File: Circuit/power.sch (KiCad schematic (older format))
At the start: 20 parts, among them Q202 FDN340P, Q203 FDN340P, U201 CN3063, U202 MCP6002, U4 LD3985M

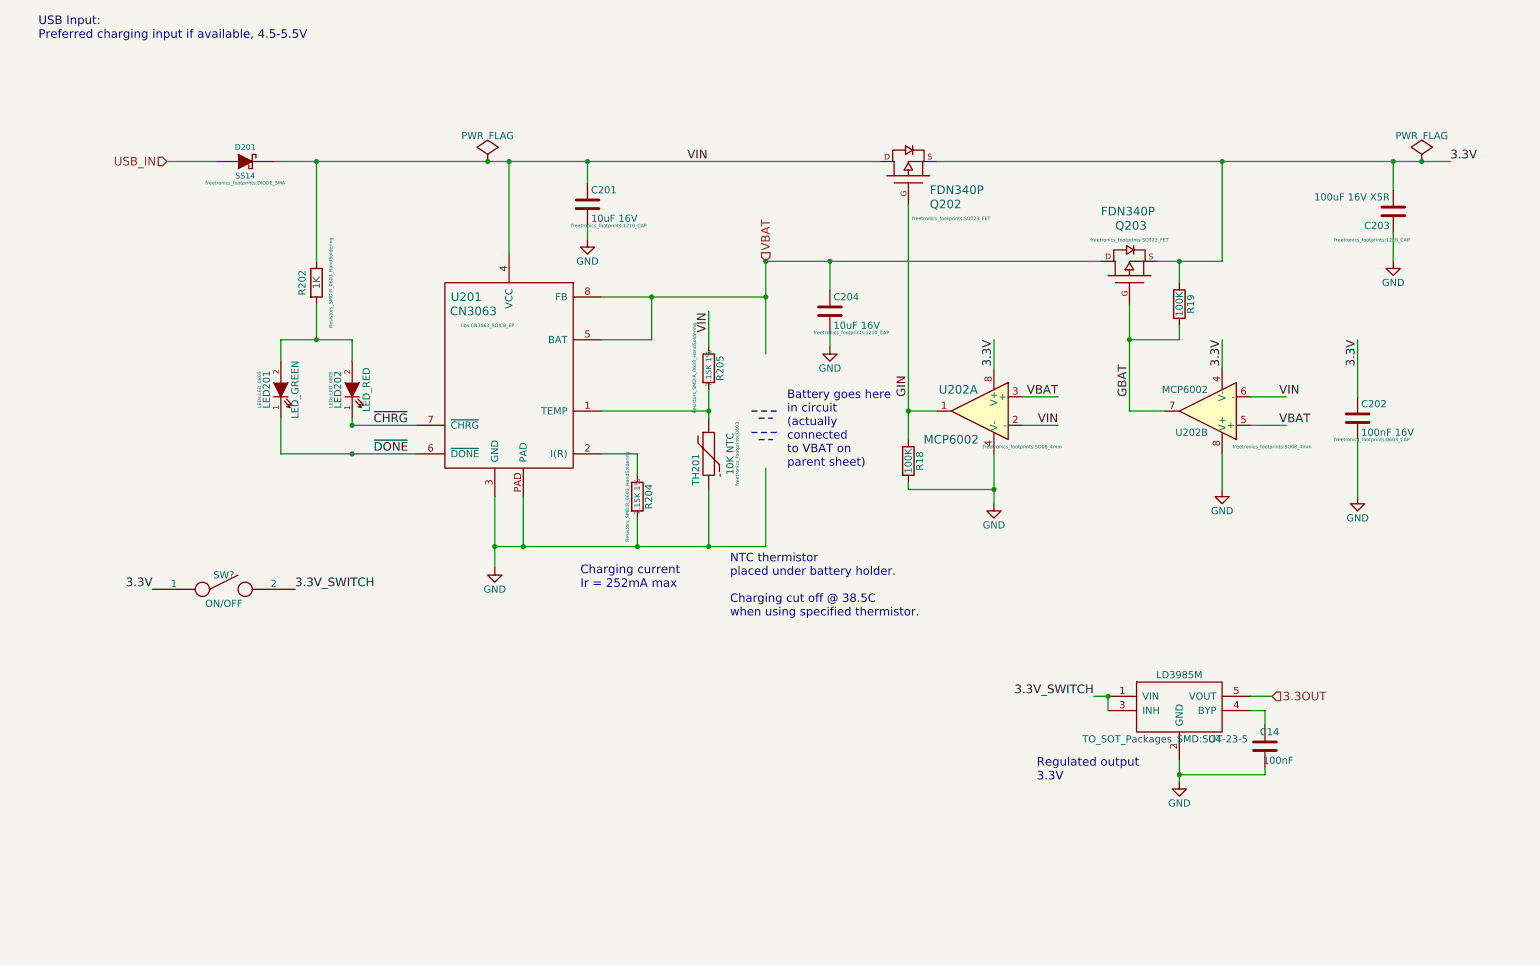
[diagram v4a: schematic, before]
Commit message: Updated pcb to start placing components.
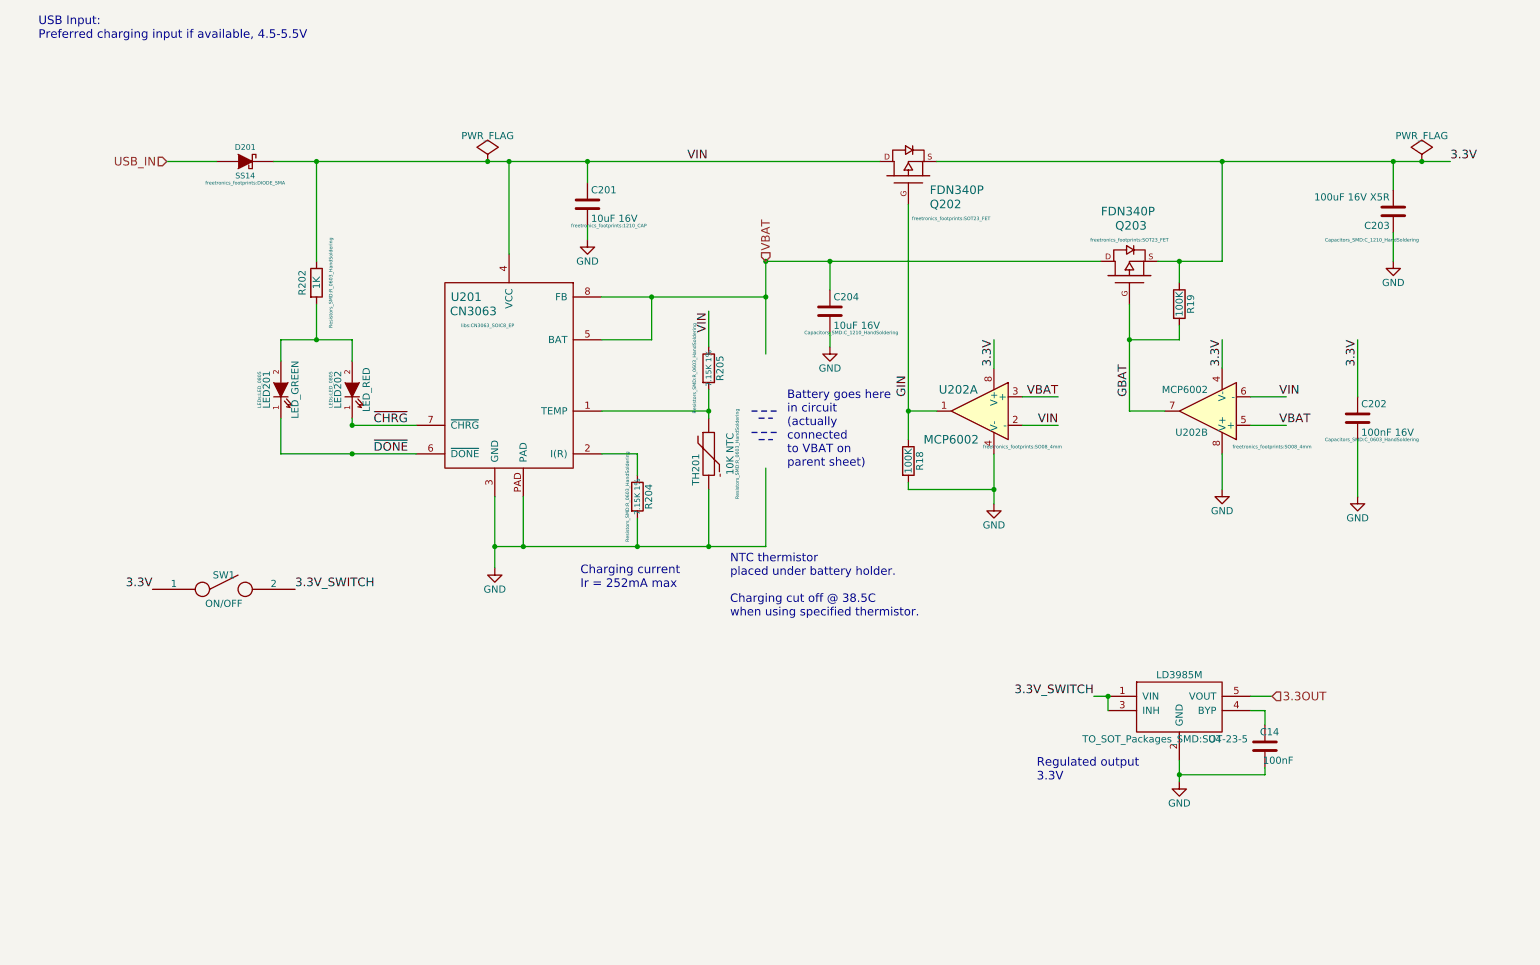
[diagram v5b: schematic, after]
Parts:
- C202: footprint freetronics_footprints:0603_CAP -> Capacitors_SMD:C_0603_HandSoldering
- C203, C204: footprint freetronics_footprints:1210_CAP -> Capacitors_SMD:C_1210_HandSoldering
- SW1: renamed from SW?; footprint (none) -> libs:SS12D00
- TH201: footprint freetronics_footprints:0603 -> Resistors_SMD:R_0603_HandSoldering
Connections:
- wire segments 86 -> 64
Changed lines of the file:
@@
 LIBS:cp2102
 LIBS:ltc3426
-LIBS:rotary
 LIBS:adxl345
 LIBS:bme280
@@
 USB_IN
 $Comp
-L GND #PWR044
+L GND #PWR032
 U 1 1 563C4E24
 P 3950 4650
-F 0 "#PWR044" H 3950 4400 50  0001 C CNN
+F 0 "#PWR032" H 3950 4400 50  0001 C CNN
 F 1 "GND" H 3950 4500 50  0000 C CNN
 F 2 "" H 3950 4650 60  0000 C CNN
@@
 Charging current\nIr = 252mA max
 $Comp
-L GND #PWR046
+L GND #PWR033
 U 1 1 56417FB3
 P 7450 4200
-F 0 "#PWR046" H 7450 3950 50  0001 C CNN
+F 0 "#PWR033" H 7450 3950 50  0001 C CNN
 F 1 "GND" H 7450 4050 50  0000 C CNN
 F 2 "" H 7450 4200 60  0000 C CNN
@@
 3.3OUT
 $Comp
-L GND #PWR047
+L GND #PWR034
 U 1 1 5641AA9F
 P 10250 2500
-F 0 "#PWR047" H 10250 2250 50  0001 C CNN
+F 0 "#PWR034" H 10250 2250 50  0001 C CNN
 F 1 "GND" H 10250 2350 50  0000 C CNN
 F 2 "" H 10250 2500 60  0000 C CNN
@@
 $EndComp
 $Comp
-L GND #PWR048
+L GND #PWR035
 U 1 1 5642C1C1
 P 9050 4100
-F 0 "#PWR048" H 9050 3850 50  0001 C CNN
+F 0 "#PWR035" H 9050 3850 50  0001 C CNN
 F 1 "GND" H 9050 3950 50  0000 C CNN
 F 2 "" H 9050 4100 60  0000 C CNN
@@
 F 0 "C203" H 10275 2250 50  0000 L CNN
 F 1 "100uF 16V X5R" H 10275 2050 50  0000 L CNN
-F 2 "freetronics_footprints:1210_CAP" H 10400 2350 24  0000 C CNN
+F 2 "Capacitors_SMD:C_1210_HandSoldering" H 10400 2350 24  0000 C CNN
 F 3 "" H 10250 2150 60  0000 C CNN
 	1    10250 2150
@@
 $EndComp
 $Comp
-L PWR_FLAG #FLG049
+L PWR_FLAG #FLG036
 U 1 1 5642D1CE
 P 10450 1800
-F 0 "#FLG049" H 10450 1895 50  0001 C CNN
+F 0 "#FLG036" H 10450 1895 50  0001 C CNN
 F 1 "PWR_FLAG" H 10450 1980 50  0000 C CNN
 F 2 "" H 10450 1800 60  0000 C CNN
@@
 $EndComp
 $Comp
-L PWR_FLAG #FLG050
+L PWR_FLAG #FLG037
 U 1 1 5642D5A3
 P 3900 1800
-F 0 "#FLG050" H 3900 1895 50  0001 C CNN
+F 0 "#FLG037" H 3900 1895 50  0001 C CNN
 F 1 "PWR_FLAG" H 3900 1980 50  0000 C CNN
 F 2 "" H 3900 1800 60  0000 C CNN
@@
 F 0 "C202" H 10025 3700 50  0000 L CNN
 F 1 "100nF 16V" H 10025 3500 50  0000 L CNN
-F 2 "freetronics_footprints:0603_CAP" H 10100 3450 24  0000 C CNN
+F 2 "Capacitors_SMD:C_0603_HandSoldering" H 10100 3450 24  0000 C CNN
 F 3 "" H 10000 3600 60  0000 C CNN
 	1    10000 3600
@@
 $EndComp
 $Comp
-L GND #PWR051
+L GND #PWR038
 U 1 1 5642DA26
 P 10000 4150
-F 0 "#PWR051" H 10000 3900 50  0001 C CNN
+F 0 "#PWR038" H 10000 3900 50  0001 C CNN
 F 1 "GND" H 10000 4000 50  0000 C CNN
 F 2 "" H 10000 4150 60  0000 C CNN
@@
 $EndComp
 $Comp
-L GND #PWR052
+L GND #PWR039
 U 1 1 5642CE9D
 P 4600 2350
-F 0 "#PWR052" H 4600 2100 50  0001 C CNN
+F 0 "#PWR039" H 4600 2100 50  0001 C CNN
 F 1 "GND" H 4600 2200 50  0000 C CNN
 F 2 "" H 4600 2350 60  0000 C CNN
@@
 	5050 3050 5050 2750
 Wire Wire Line
-	4700 2750 5050 2750
-Wire Wire Line
-	5050 2750 5850 2750
+	4700 2750 5850 2750
 Wire Wire Line
 	4700 3550 5450 3550
@@
 Connection ~ 4050 1800
 Wire Wire Line
-	2400 1800 2700 1800
-Wire Wire Line
-	2700 1800 3900 1800
-Wire Wire Line
-	3900 1800 4050 1800
-Wire Wire Line
-	4050 1800 4600 1800
-Wire Wire Line
-	4600 1800 6650 1800
+	2400 1800 6650 1800
 Wire Wire Line
 	2950 3650 3400 3650
@@
 Connection ~ 2950 3850
 Wire Wire Line
-	6850 2100 6850 3550
-Wire Wire Line
-	6850 3550 6850 3750
-Wire Wire Line
-	2450 3850 2950 3850
-Wire Wire Line
-	2950 3850 3400 3850
+	6850 2100 6850 3750
+Wire Wire Line
+	2450 3850 3400 3850
 Wire Wire Line
 	2450 3050 2450 3200
@@
 Connection ~ 4950 4500
 Wire Wire Line
-	5850 2500 6300 2500
-Wire Wire Line
-	6300 2500 8200 2500
-Wire Wire Line
-	8400 2800 8400 3050
-Wire Wire Line
-	8400 3050 8400 3550
+	5850 2500 8200 2500
+Wire Wire Line
+	8400 2800 8400 3550
 Connection ~ 9050 1800
 Wire Wire Line
-	8600 2500 8750 2500
-Wire Wire Line
-	8750 2500 9050 2500
-Wire Wire Line
-	7050 1800 9050 1800
-Wire Wire Line
-	9050 1800 10250 1800
-Wire Wire Line
-	10250 1800 10450 1800
-Wire Wire Line
-	10450 1800 10650 1800
+	8600 2500 9050 2500
+Wire Wire Line
+	7050 1800 10650 1800
 Wire Wire Line
 	10250 1800 10250 2000
@@
 	10250 2300 10250 2500
 Wire Wire Line
-	7450 3850 7450 4100
-Wire Wire Line
-	7450 4100 7450 4200
+	7450 3850 7450 4200
 Wire Wire Line
 	9050 2500 9050 1800
@@
 F 0 "TH201" V 5360 3740 50  0000 C CNN
 F 1 "10K NTC" V 5600 3850 50  0000 C CNN
-F 2 "freetronics_footprints:0603" V 5650 3850 24  0000 C CNN
+F 2 "Resistors_SMD:R_0603_HandSoldering" V 5650 3850 24  0000 C CNN
 F 3 "http://www.murata.com/products/catalog/pdf/r44e.pdf" H 5450 3850 60  0001 C CNN
 F 4 "NCP18XH103F03RB" V 5450 3850 60  0001 C CNN "MPN"
@@
 VIN
 Wire Wire Line
-	5450 3400 5450 3550
-Wire Wire Line
-	5450 3550 5450 3600
+	5450 3400 5450 3600
 Connection ~ 5450 3550
 Wire Wire Line
@@
 	2700 2800 2700 3050
 Wire Wire Line
-	2450 3050 2700 3050
-Wire Wire Line
-	2700 3050 2950 3050
+	2450 3050 2950 3050
 Connection ~ 2700 3050
 $Comp
@@
 F 0 "C204" H 6325 2950 50  0000 L CNN
 F 1 "10uF 16V" H 6325 2750 50  0000 L CNN
-F 2 "freetronics_footprints:1210_CAP" H 6450 2700 24  0000 C CNN
+F 2 "Capacitors_SMD:C_1210_HandSoldering" H 6450 2700 24  0000 C CNN
 F 3 "" H 6300 2850 60  0000 C CNN
 	1    6300 2850
@@
 	6300 3000 6300 3100
 $Comp
-L GND #PWR053
+L GND #PWR040
 U 1 1 566FA00B
 P 6300 3100
-F 0 "#PWR053" H 6300 2850 50  0001 C CNN
+F 0 "#PWR040" H 6300 2850 50  0001 C CNN
 F 1 "GND" H 6300 2950 50  0000 C CNN
 F 2 "" H 6300 3100 60  0000 C CNN
@@
 $EndComp
 Wire Wire Line
-	3950 4500 4150 4500
-Wire Wire Line
-	4150 4500 4950 4500
-Wire Wire Line
-	4950 4500 5450 4500
-Wire Wire Line
-	5450 4500 5850 4500
-Wire Wire Line
-	3950 4150 3950 4500
-Wire Wire Line
-	3950 4500 3950 4650
+	3950 4500 5850 4500
+Wire Wire Line
+	3950 4150 3950 4650
 Wire Wire Line
 	4150 4500 4150 4150
@@
 VBAT
 Wire Wire Line
-	5850 2500 5850 2750
-Wire Wire Line
-	5850 2750 5850 3150
+	5850 2500 5850 3150
 $Comp
 L R R18
@@
 	9350 6100 8750 6100
 Wire Wire Line
-	8750 6000 8750 6100
-Wire Wire Line
-	8750 6100 8750 6150
+	8750 6000 8750 6150
 Wire Wire Line
 	8250 5650 8250 5550
@@
 	9250 5550 9400 5550
 $Comp
-L GND #PWR056
+L GND #PWR041
 U 1 1 57FB3009
 P 8750 6150
-F 0 "#PWR056" H 8750 5900 50  0001 C CNN
+F 0 "#PWR041" H 8750 5900 50  0001 C CNN
 F 1 "GND" H 8750 6000 50  0000 C CNN
 F 2 "" H 8750 6150 50  0000 C CNN
@@
 3.3V
 $Comp
-L SPST SW?
+L SPST SW1
 U 1 1 5810B231
 P 2050 4800
-F 0 "SW?" H 2050 4900 50  0000 C CNN
+F 0 "SW1" H 2050 4900 50  0000 C CNN
 F 1 "ON/OFF" H 2050 4700 50  0000 C CNN
-F 2 "" H 2050 4800 50  0000 C CNN
+F 2 "libs:SS12D00" H 2050 4800 50  0001 C CNN
 F 3 "" H 2050 4800 50  0000 C CNN
 	1    2050 4800

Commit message: Some notes & adding sheets.
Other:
- note added: "Charge done not necessary? \nI'd just turn off the ~CHRG~ LED\n and call it good."
- note added: "Insufficient current capability."
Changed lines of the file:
@@
 $Descr A4 11693 8268
 encoding utf-8
-Sheet 2 4
+Sheet 2 7
 Title ""
 Date ""
@@
 Wire Wire Line
 	1650 1800 2000 1800
+Text Notes 800  3800 0    60   ~ 0
+Charge done not necessary? \nI'd just turn off the ~CHRG~ LED\n and call it good.
+Wire Notes Line
+	750  3000 2650 3000
+Wire Notes Line
+	2650 3000 2650 4250
+Wire Notes Line
+	2650 4250 750  4250
+Wire Notes Line
+	750  4250 750  3000
+Wire Notes Line
+	7400 5050 7400 6450
+Wire Notes Line
+	7400 6450 10100 6450
+Wire Notes Line
+	10100 6450 10100 5050
+Wire Notes Line
+	10100 5050 7400 5050
+Text Notes 7400 5000 0    60   ~ 0
+Insufficient current capability.
 $EndSCHEMATC

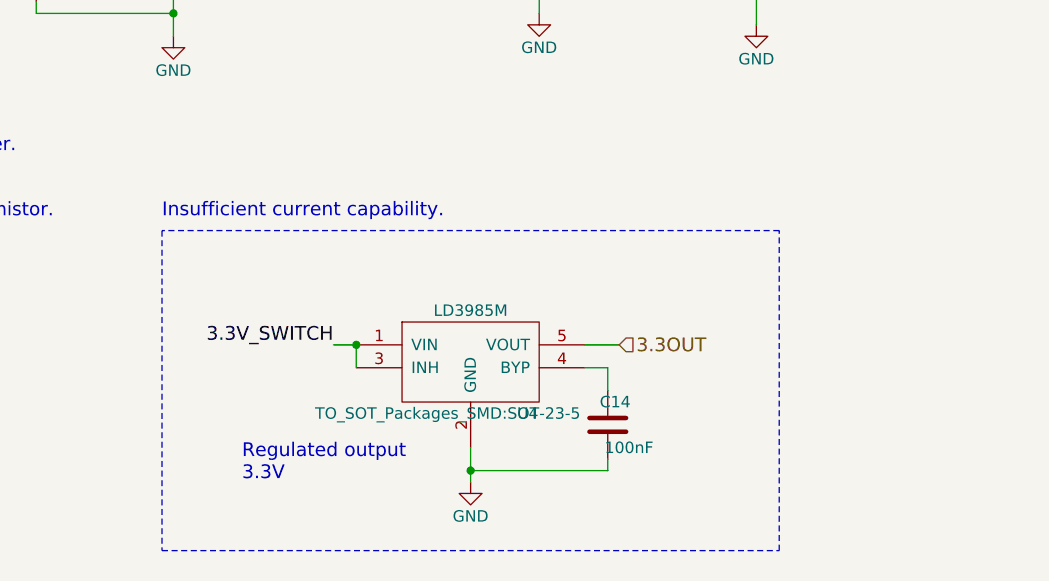
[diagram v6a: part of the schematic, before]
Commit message: Changed 3v3 regulator to higher current buck converter.
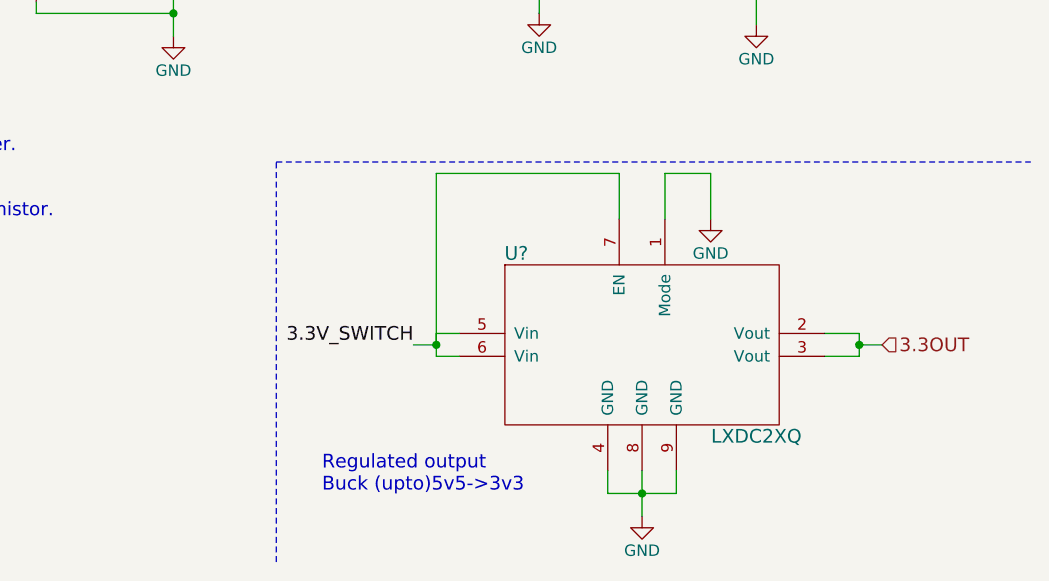
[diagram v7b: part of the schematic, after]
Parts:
- removed C14: 100nF, freetronics_footprints:1210_CAP, symbol C
- removed U4: LD3985M, TO_SOT_Packages_SMD:SOT-23-5, symbol LD3985M
- added U?: LXDC2XQ, IoTuz:LXDC2XQ, symbol LXDC2XQ
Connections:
- wire segments 64 -> 74
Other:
- note added: "Regulated output\nBuck (upto)5v5->3v3"
- note removed: "Insufficient current capability."
- note removed: "Regulated output\n3.3V"

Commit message: Output cap on buck.
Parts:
- added C12: 10uF, symbol CAP
- gave numbers to parts that had none: 1
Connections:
- wire segments 74 -> 77
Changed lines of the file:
@@
 USB_IN
 $Comp
-L GND #PWR032
+L GND #PWR32
 U 1 1 563C4E24
 P 3950 4650
-F 0 "#PWR032" H 3950 4400 50  0001 C CNN
+F 0 "#PWR32" H 3950 4400 50  0001 C CNN
 F 1 "GND" H 3950 4500 50  0000 C CNN
 F 2 "" H 3950 4650 60  0000 C CNN
@@
 Charging current\nIr = 252mA max
 $Comp
-L GND #PWR033
+L GND #PWR35
 U 1 1 56417FB3
 P 7450 4200
-F 0 "#PWR033" H 7450 3950 50  0001 C CNN
+F 0 "#PWR35" H 7450 3950 50  0001 C CNN
 F 1 "GND" H 7450 4050 50  0000 C CNN
 F 2 "" H 7450 4200 60  0000 C CNN
@@
 3.3OUT
 $Comp
-L GND #PWR034
+L GND #PWR40
 U 1 1 5641AA9F
 P 10250 2500
-F 0 "#PWR034" H 10250 2250 50  0001 C CNN
+F 0 "#PWR40" H 10250 2250 50  0001 C CNN
 F 1 "GND" H 10250 2350 50  0000 C CNN
 F 2 "" H 10250 2500 60  0000 C CNN
@@
 $EndComp
 $Comp
-L GND #PWR035
+L GND #PWR36
 U 1 1 5642C1C1
 P 9050 4100
-F 0 "#PWR035" H 9050 3850 50  0001 C CNN
+F 0 "#PWR36" H 9050 3850 50  0001 C CNN
 F 1 "GND" H 9050 3950 50  0000 C CNN
 F 2 "" H 9050 4100 60  0000 C CNN
@@
 $EndComp
 $Comp
-L PWR_FLAG #FLG036
+L PWR_FLAG #FLG2
 U 1 1 5642D1CE
 P 10450 1800
-F 0 "#FLG036" H 10450 1895 50  0001 C CNN
+F 0 "#FLG2" H 10450 1895 50  0001 C CNN
 F 1 "PWR_FLAG" H 10450 1980 50  0000 C CNN
 F 2 "" H 10450 1800 60  0000 C CNN
@@
 $EndComp
 $Comp
-L PWR_FLAG #FLG037
+L PWR_FLAG #FLG1
 U 1 1 5642D5A3
 P 3900 1800
-F 0 "#FLG037" H 3900 1895 50  0001 C CNN
+F 0 "#FLG1" H 3900 1895 50  0001 C CNN
 F 1 "PWR_FLAG" H 3900 1980 50  0000 C CNN
 F 2 "" H 3900 1800 60  0000 C CNN
@@
 $EndComp
 $Comp
-L GND #PWR038
+L GND #PWR39
 U 1 1 5642DA26
 P 10000 4150
-F 0 "#PWR038" H 10000 3900 50  0001 C CNN
+F 0 "#PWR39" H 10000 3900 50  0001 C CNN
 F 1 "GND" H 10000 4000 50  0000 C CNN
 F 2 "" H 10000 4150 60  0000 C CNN
@@
 $EndComp
 $Comp
-L GND #PWR039
+L GND #PWR33
 U 1 1 5642CE9D
 P 4600 2350
-F 0 "#PWR039" H 4600 2100 50  0001 C CNN
+F 0 "#PWR33" H 4600 2100 50  0001 C CNN
 F 1 "GND" H 4600 2200 50  0000 C CNN
 F 2 "" H 4600 2350 60  0000 C CNN
@@
 $EndComp
 $Comp
-L GND #PWR040
+L GND #PWR34
 U 1 1 566FA00B
 P 6300 3100
-F 0 "#PWR040" H 6300 2850 50  0001 C CNN
+F 0 "#PWR34" H 6300 2850 50  0001 C CNN
 F 1 "GND" H 6300 2950 50  0000 C CNN
 F 2 "" H 6300 3100 60  0000 C CNN
@@
 Charge done not necessary? \nI'd just turn off the ~CHRG~ LED\n and call it good.
 $Comp
-L LXDC2XQ U?
+L LXDC2XQ U3
 U 1 1 5812C4CE
 P 9500 5550
-F 0 "U?" H 8950 5950 60  0000 C CNN
+F 0 "U3" H 8950 5950 60  0000 C CNN
 F 1 "LXDC2XQ" H 10000 5150 60  0000 C CNN
 F 2 "IoTuz:LXDC2XQ" H 9500 5550 60  0001 C CNN
@@
 $EndComp
 $Comp
-L GND #PWR?
+L GND #PWR37
 U 1 1 5812C93A
 P 9500 6300
-F 0 "#PWR?" H 9500 6050 50  0001 C CNN
+F 0 "#PWR37" H 9500 6050 50  0001 C CNN
 F 1 "GND" H 9500 6150 50  0000 C CNN
 F 2 "" H 9500 6300 60  0000 C CNN
@@
 $EndComp
 $Comp
-L GND #PWR?
+L GND #PWR38
 U 1 1 5812E212
 P 9800 5000
-F 0 "#PWR?" H 9800 4750 50  0001 C CNN
+F 0 "#PWR38" H 9800 4750 50  0001 C CNN
 F 1 "GND" H 9800 4850 50  0000 C CNN
 F 2 "" H 9800 5000 60  0000 C CNN
@@
 	1    0    0    -1
 $EndComp
+$Comp
+L CAP C12
+U 1 1 5812F47A
+P 10450 5900
+F 0 "C12" H 10500 6000 50  0000 L CNN
+F 1 "10uF" H 10500 5800 50  0000 L CNN
+F 2 "" H 10450 5900 60  0000 C CNN
+F 3 "" H 10450 5900 60  0000 C CNN
+	1    10450 5900
+	1    0    0    -1
+$EndComp
 Wire Wire Line
 	5050 3050 5050 2750
@@
 Wire Notes Line
 	7900 4750 11200 4750
+Wire Wire Line
+	10450 5550 10450 5700
+Wire Wire Line
+	10450 6100 10450 6200
+Wire Wire Line
+	10450 6200 9500 6200
 $EndSCHEMATC
